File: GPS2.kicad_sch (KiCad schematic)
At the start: 1 part, among them J5 Conn_01x05_Pin

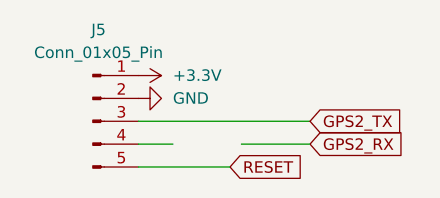
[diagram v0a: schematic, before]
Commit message: began fixing schematic added barometer
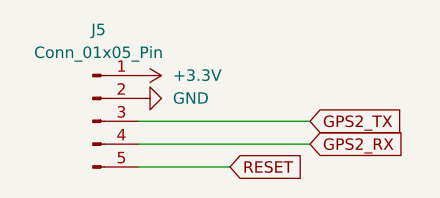
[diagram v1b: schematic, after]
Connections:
- net GPS2_RX: now also J5.4 (Pin_4)
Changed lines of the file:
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@@
 	(wire
 		(pts
-			(xy 120.65 74.93) (xy 116.84 74.93)
+			(xy 116.84 74.93) (xy 135.89 74.93)
 		)
 		(stroke
@@
 		)
 		(stroke
-			(width 0)
-			(type default)
-		)
-	)
-	(wire
-		(pts
-			(xy 135.89 74.93) (xy 128.27 74.93)
-		)
-		(stroke
